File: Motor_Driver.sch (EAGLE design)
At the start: 20 parts, among them T1 2N3904, T2 2N3904

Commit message: Increased space between MOSFETs to allow for proper heatsink size
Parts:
- removed Q5: (no value), transistor-power:PMOSFET_PTO220BV
- removed X2: (no value), con-wago-500:W237-4
- added Q1: (no value), transistor-power:PMOSFET_NTO220BV
- added X1: M_B V+ GND M_A, MyParts:W237-4
- Q2, Q3: device transistor-power:PMOSFET_NTO220BV -> transistor-power:PMOSFET_PTO220BV
- Q4: device transistor-power:PMOSFET_PTO220BV -> transistor-power:PMOSFET_NTO220BV
- R2, R5: value 10k -> 1k
- R3, R6: value 1k -> 10k
- SV1: value (none) -> INPUT_HEADER; device con-lstb:MA04-1 -> MyParts:MA04-1
- renumbered R7 to R1
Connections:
- net +12V: now also D2.C, D3.C, Q2.S, Q3.S, R2.2, X1-2.KL; no longer D1.C, D4.C, Q4.S, Q5.S, R6.2, X2-2.KL
- net DRIVE_A: now also Q3.G, R2.1, R6.2, T2.C; no longer Q2.G, R2.2, R6.1, T1.C
- net DRIVE_B: now also Q1.G, Q2.G, R3.2, T1.C; no longer Q3.G, Q5.G, R5.2, T2.C
- net GND: now also D1.A, D4.A, Q1.S, Q4.S, R3.1, R6.1, X1-3.KL; no longer D2.A, D3.A, Q2.S, Q3.S, R2.1, R5.1, X2-3.KL
- net INPUT_A: now also R5.2, T2.B; no longer R3.2, T1.B
- net INPUT_B: now also T1.B; no longer T2.B
- net M_DRIVE_A: now also D3.A, D4.C, Q3.D, X1-4.KL; no longer D1.A, D2.C, Q2.D, X2-4.KL
- net M_DRIVE_B: now also D1.C, D2.A, Q1.D, Q2.D, X1-1.KL; no longer D3.C, D4.A, Q3.D, Q5.D, X2-1.KL
- net N$2: now also LED2.A, R5.1; no longer LED1.A, R3.1
- net N$4: now also LED1.A; no longer LED2.A
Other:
- moved on the sheet: D1, D2, D3, D4, LED1, LED2, R2, R3, R5, R6, SV1, T1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

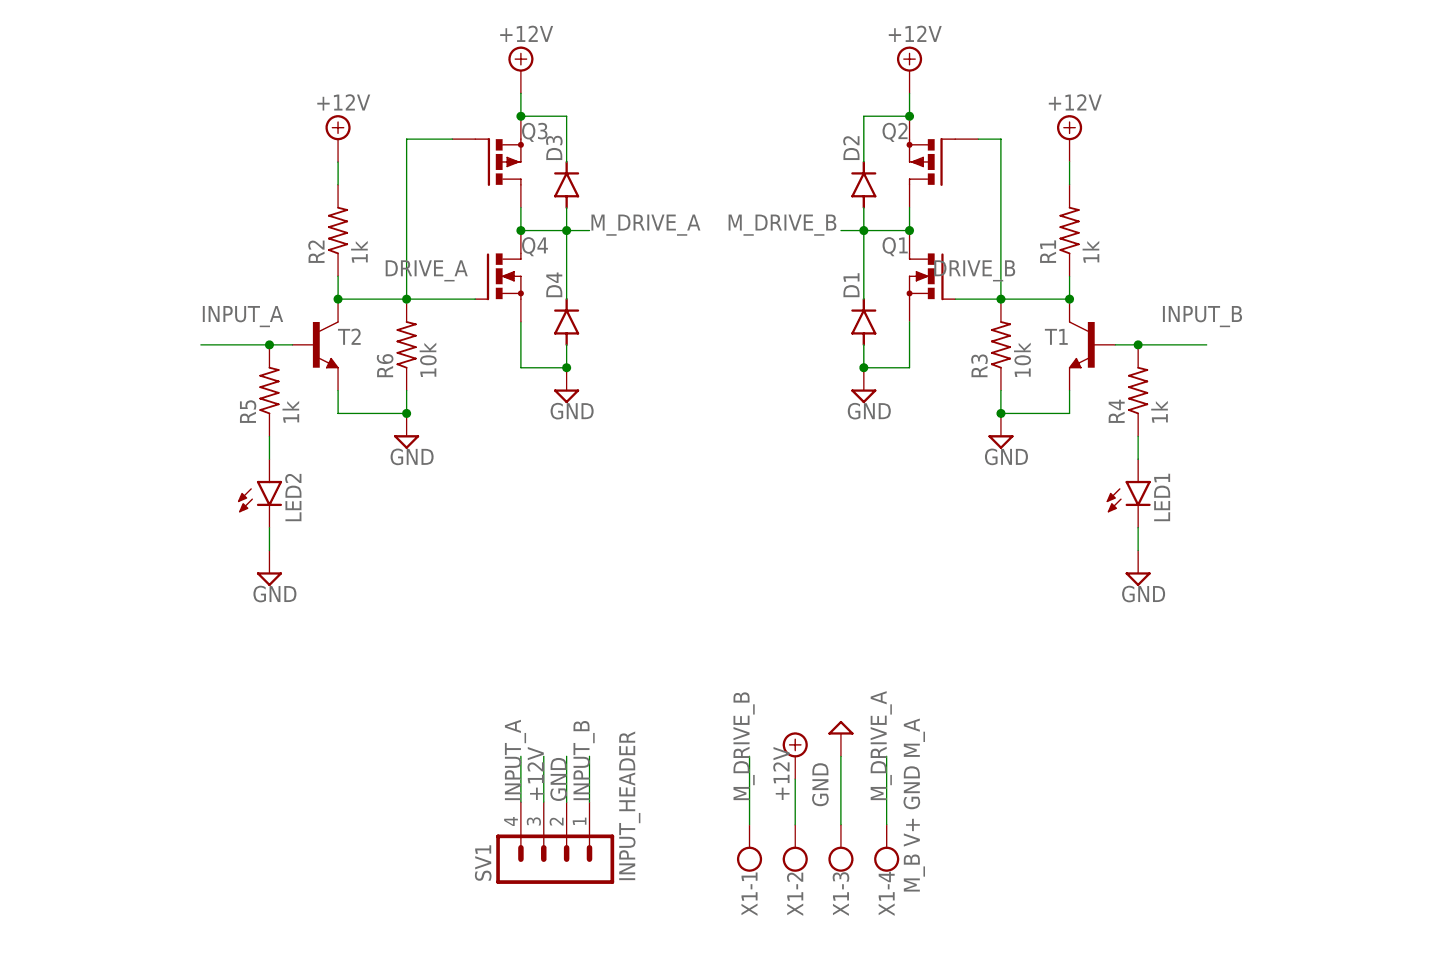
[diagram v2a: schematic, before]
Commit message: Added resistors to the base of the input resistors
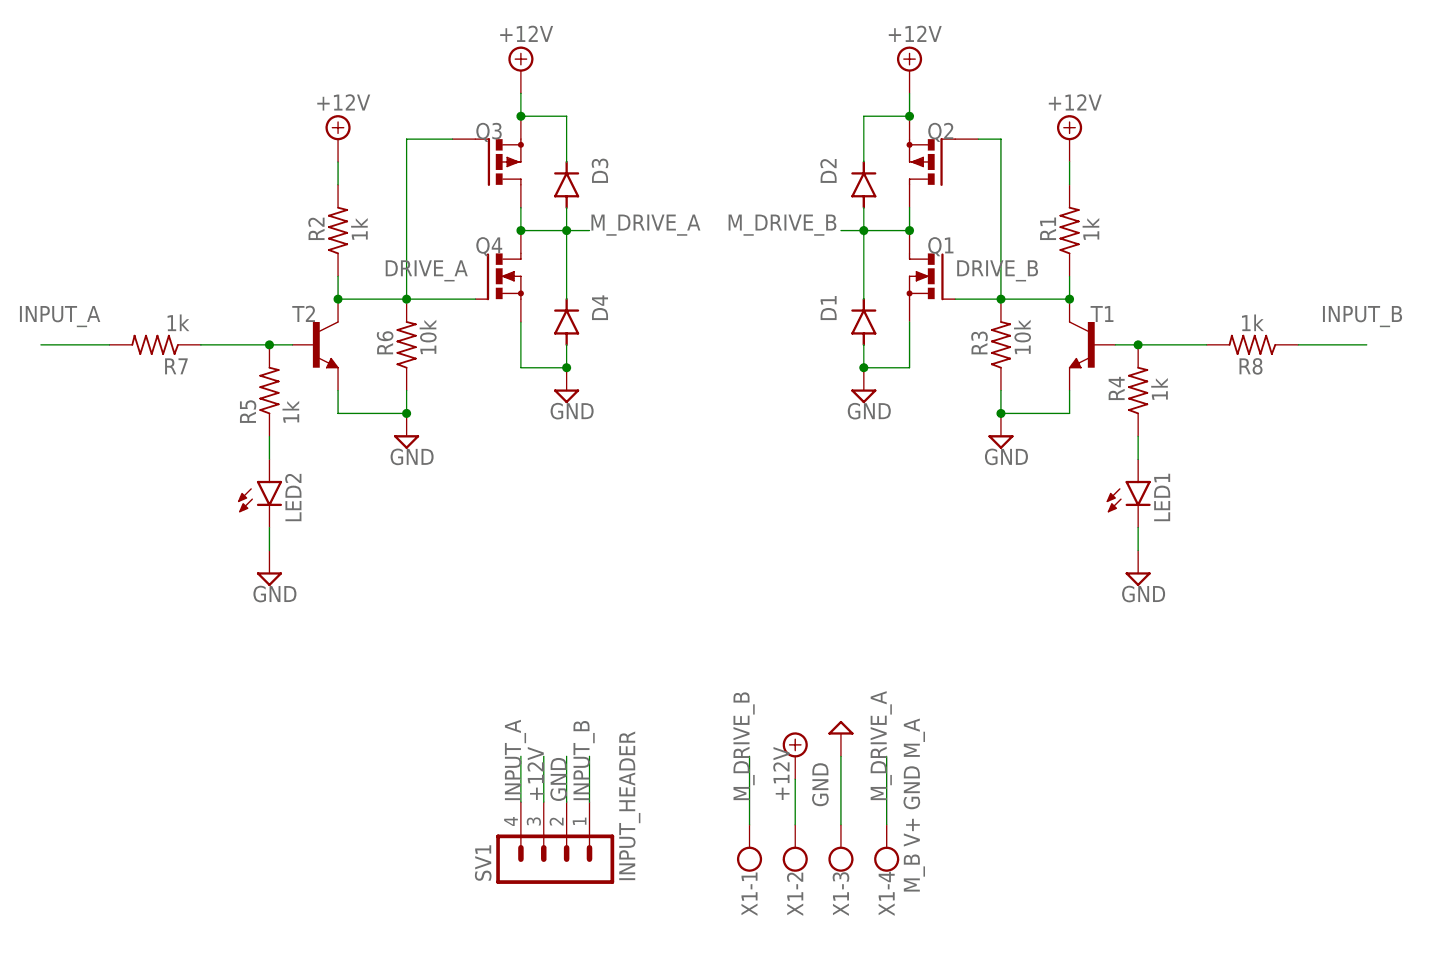
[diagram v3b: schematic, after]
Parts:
- added R7, R8: 1k, resistor:R-US_0207/10
- LED1: value (none) -> LED_B
- LED2: value (none) -> LED_A
- Q1: value (none) -> N_B
- Q2: value (none) -> P_B
- Q3: value (none) -> P_A
- Q4: value (none) -> N_A
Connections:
- new net N$1: R5.2, R7.1, T2.B
- new net N$3: R4.2, R8.2, T1.B
- net INPUT_A: now also R7.2; no longer R5.2, T2.B
- net INPUT_B: now also R8.1; no longer R4.2, T1.B
